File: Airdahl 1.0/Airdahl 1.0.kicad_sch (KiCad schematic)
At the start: 65 parts, among them J1 Conn_01x04, J2 DF40C-34DS-0.4V_58_, J3 DF40C-34DS-0.4V_58_, J4 USB_C_Receptacle_USB2.0_16P, SW1 SW_MEC_5E, SW2 SW_MEC_5E, U1 STM32F446RETx, U2 MCP2200-I-MQ, U7 NCP1117-3.3_SOT223, Y1 ABM3B-8.000MHZ-12-D1X-T, Y2 ABS25-32.768KHZ-6-T, Y3 12MHz

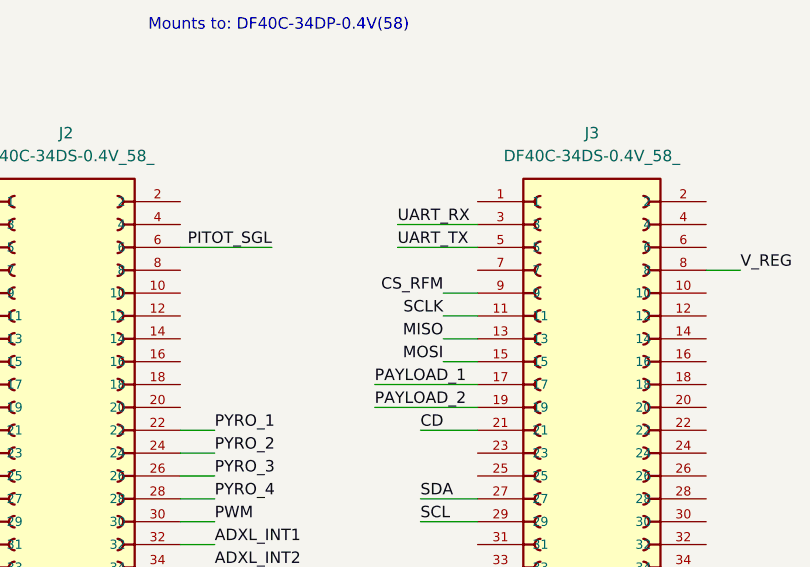
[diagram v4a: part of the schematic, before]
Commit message: added pinouts for board interface, b3b xh servo connector and 6v buck to ace carrier
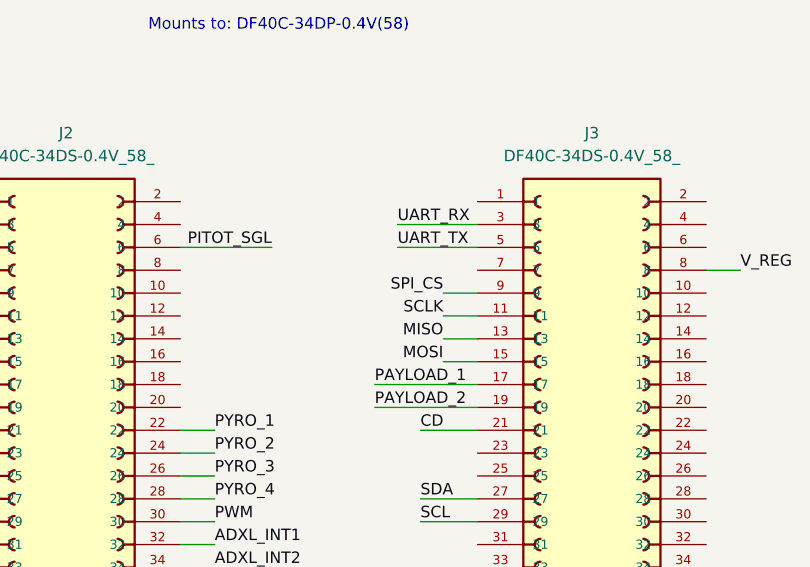
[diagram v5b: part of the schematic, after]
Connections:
- net CS_RFM: no longer J3.9
- new net SPI_CS: J3.9
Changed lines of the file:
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@@
 		)
 	)
-	(label "CS_RFM"
+	(label "SPI_CS"
 		(at 88.9 236.22 180)
 		(effects

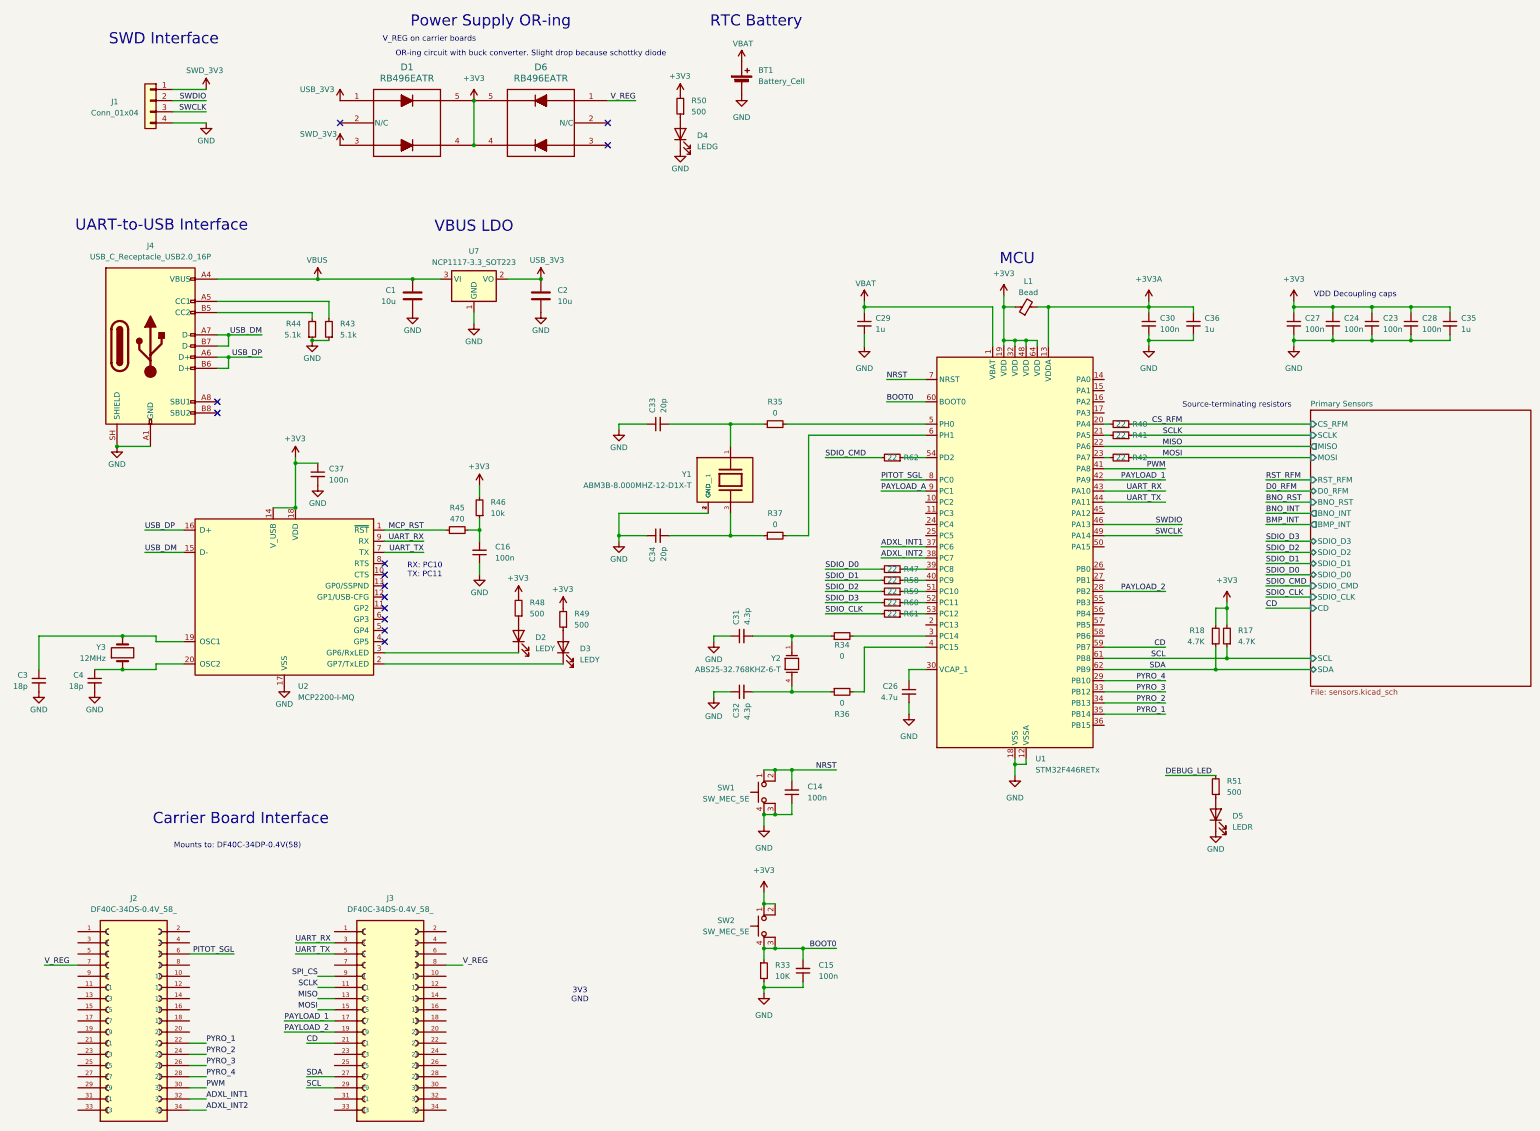
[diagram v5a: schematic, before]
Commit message: added remaining unused gpio to carrier board interface on mainboard schematic
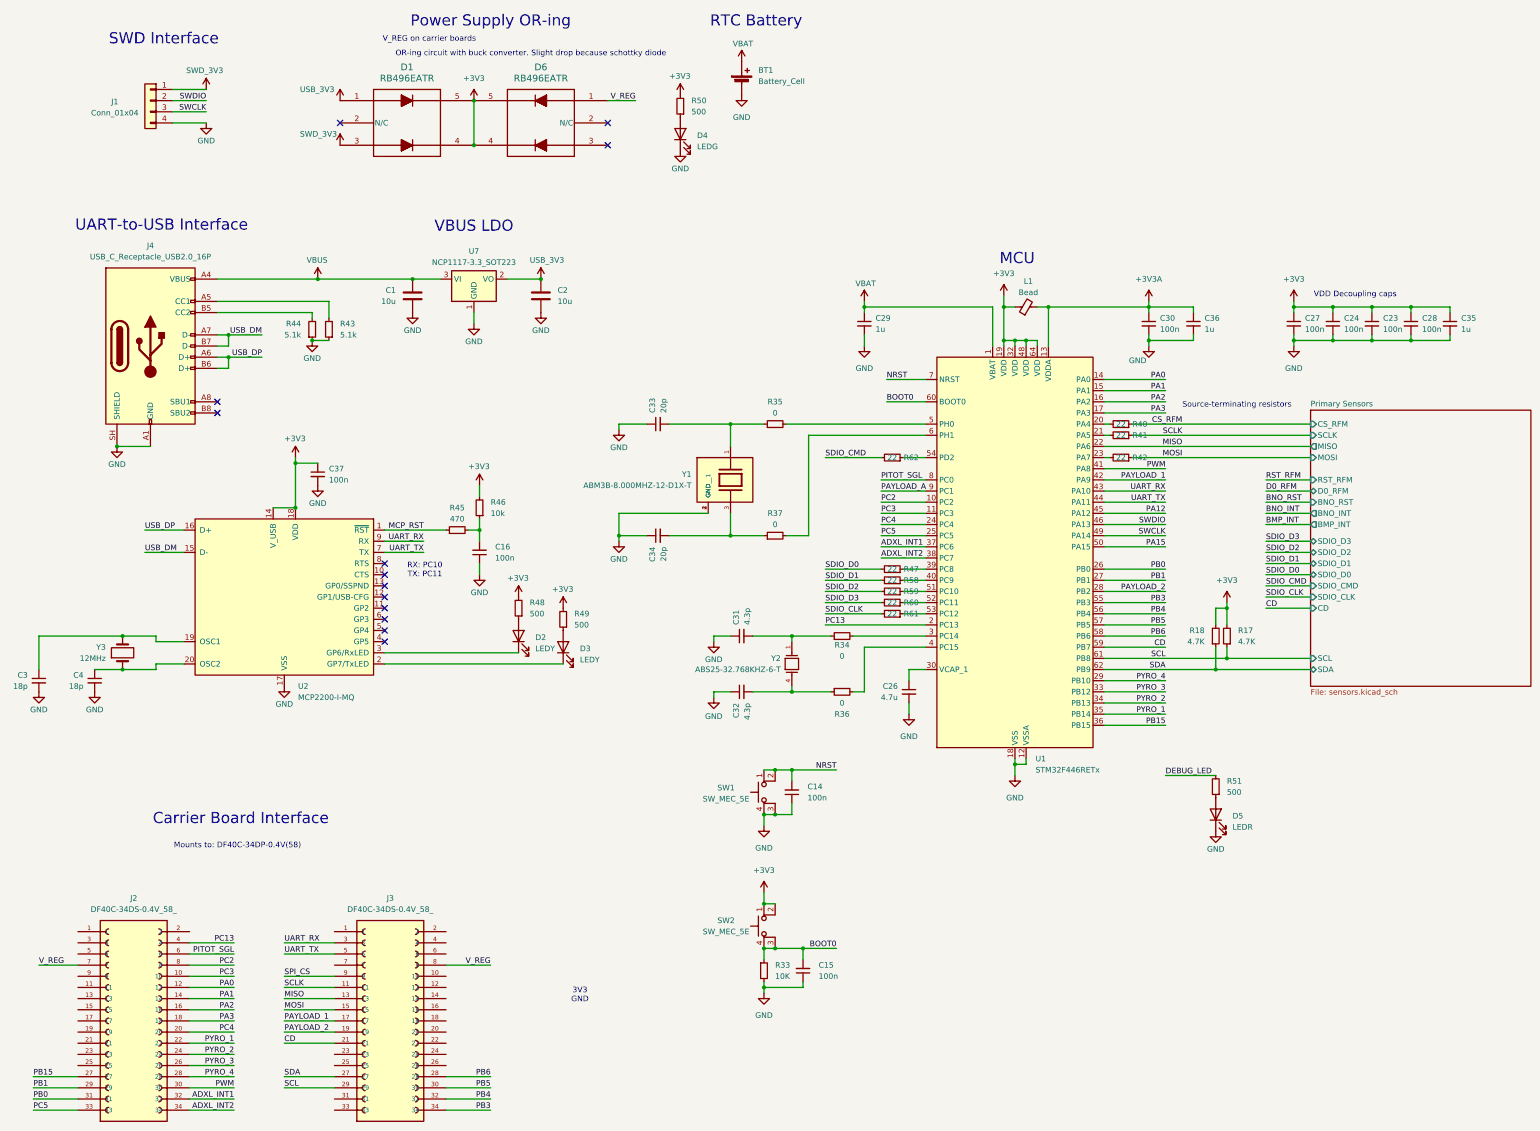
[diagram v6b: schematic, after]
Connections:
- net PC3: now reaches J2.10
- net PC3: now also U1.11 (PC3)
- net PA0: now reaches J2.12
- net PA0: now also U1.14 (PA0)
- net PA1: now reaches J2.14
- net PA1: now also U1.15 (PA1)
- net PA2: now reaches J2.16
- net PA2: now also U1.16 (PA2)
- net PA3: now reaches J2.18
- net PA3: now also U1.17 (PA3)
- net PC4: now reaches J2.20
- net PC4: now also U1.24 (PC4)
- net PB15: now reaches J2.27
- net PB15: now also U1.36 (PB15)
- net PB1: now reaches J2.29
- net PB1: now also U1.27 (PB1)
- net PB0: now reaches J2.31
- net PB0: now also U1.26 (PB0)
- net PC5: now reaches J2.33
- net PC5: now also U1.25 (PC5)
- net PC13: now reaches J2.4
- net PC13: now also U1.2 (PC13)
- net PC2: now reaches J2.8
- net PC2: now also U1.10 (PC2)
- net PB6: now reaches J3.28
- net PB6: now also U1.58 (PB6)
- net PB5: now reaches J3.30
- net PB5: now also U1.57 (PB5)
- net PB4: now reaches J3.32
- net PB4: now also U1.56 (PB4)
- net PB3: now reaches J3.34
- net PB3: now also U1.55 (PB3)
- net PA12: now reaches U1.45 (PA12)
- net PA15: now reaches U1.50 (PA15)

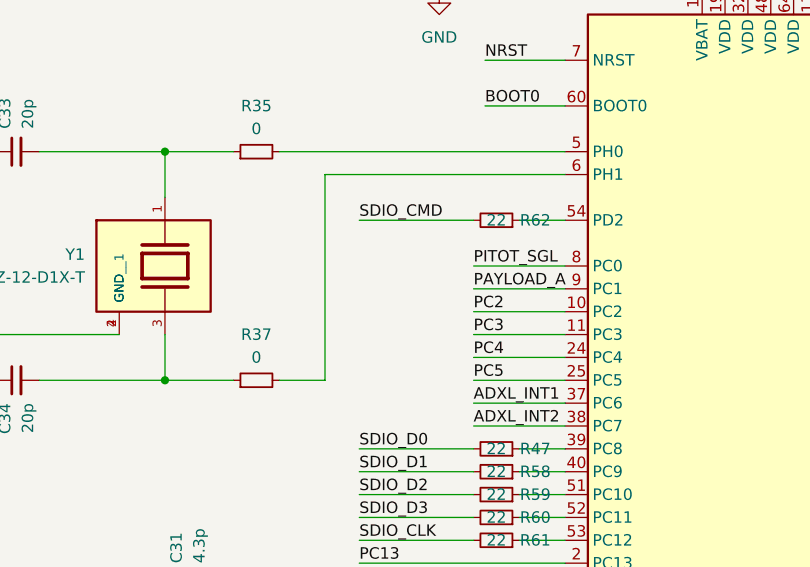
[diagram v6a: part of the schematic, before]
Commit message: adc filtering caps
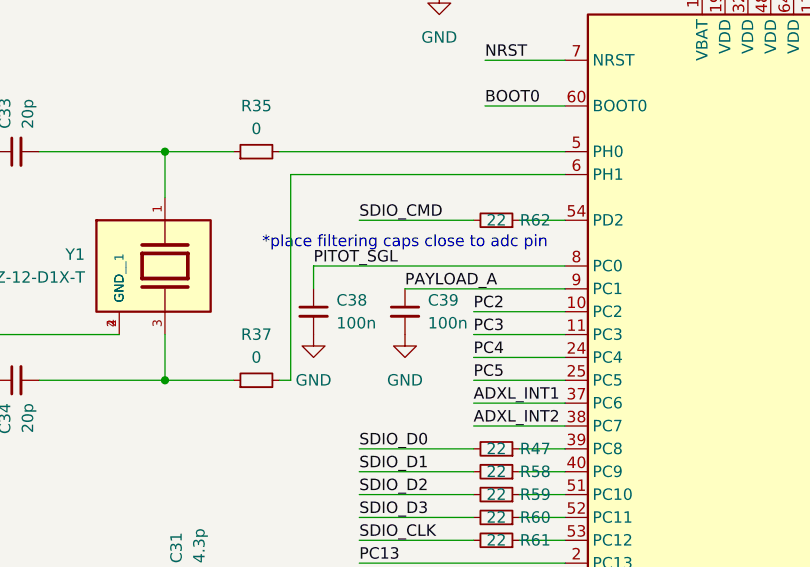
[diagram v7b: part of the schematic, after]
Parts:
- added C38, C39: 100n, Capacitor_SMD:C_0603_1608Metric_Pad1.08x0.95mm_HandSolder, symbol Device:C_Small
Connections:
- net GND: now also C38.2, C39.2
- net PAYLOAD_A: now also C39.1
- net PITOT_SGL: now also C38.1
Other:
- note added: "*place filtering caps close to adc pin"

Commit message: H-Bridge wiring + motor ports, cleaned up carrier schematics, added MISO source terminating resistors on carriers
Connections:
- net CD: no longer J3.21
- net PAYLOAD_A: now also J2.2
- net UART_RX: no longer U1.43 (PA10)
- net PAYLOAD_1 renamed PAYLOAD_1F
- net PAYLOAD_2 renamed PAYLOAD_1R
- net PAYLOAD_1R: now also U1.43 (PA10); no longer U1.28 (PB2)
- net PB0 renamed PAYLOAD_2F
- net PB1 renamed PAYLOAD_2R
- net V_REG renamed +3V3_REG
- new net PB2: U1.28 (PB2)
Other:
- note added: "*PB2 =BOOT1"
